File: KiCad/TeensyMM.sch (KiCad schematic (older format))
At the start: 13 parts, among them J1 MICROMOD-2222, U1 MK20DX256VLH7, U2 MKL02Z32VFG4, Y2 16MHz

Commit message: wip
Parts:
- removed JP1: SolderJumper_2_Open, Jumper:SolderJumper-2_P1.3mm_Open_RoundedPad1.0x1.5mm, symbol Jumper:SolderJumper_2_Open
- added JP1: SolderJumper_3_Open, Jumper:SolderJumper-3_P1.3mm_Open_RoundedPad1.0x1.5mm, symbol Jumper:SolderJumper_3_Open
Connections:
- net labels added: CTS, D3_CTX, D4_CRX, RTS
- net labels removed: EN
- wire segments 176 -> 181
- no-connect marks 44 -> 41
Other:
- note added: "Deactivates \nMKL02"
- note removed: "Close JP1 \nfor JTAG use\n(deactivates MKL02)"
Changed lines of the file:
@@
 Text GLabel 11600 4300 1    50   Input ~ 0
 SWD_DIO
-Text Notes 13100 4200 2    39   ~ 0
-Close JP1 \nfor JTAG use\n(deactivates MKL02)
+Text Notes 12700 4150 0    39   ~ 0
+Deactivates \nMKL02
 $Comp
 L power:GND #PWR013
@@
 	1    12800 4300
 	0    1    1    0
-$EndComp
-$Comp
-L Jumper:SolderJumper_2_Open JP1
-U 1 1 60214C71
-P 13000 4300
-F 0 "JP1" H 13000 4200 50  0000 C CNN
-F 1 "SolderJumper_2_Open" H 12450 4900 50  0001 C CNN
-F 2 "Jumper:SolderJumper-2_P1.3mm_Open_RoundedPad1.0x1.5mm" H 13000 4300 50  0001 C CNN
-F 3 "~" H 13000 4300 50  0001 C CNN
-	1    13000 4300
-	1    0    0    -1
 $EndComp
 Wire Wire Line
@@
 Text Label 10300 4900 0    50   ~ 0
 PTA7
-Wire Wire Line
-	13200 4300 13150 4300
-Wire Wire Line
-	12850 4300 12800 4300
-Text Label 13100 4300 0    50   ~ 0
-EN
 Text Label 10300 4700 0    50   ~ 0
 PTA6
@@
 NoConn ~ 4350 3400
 NoConn ~ 4350 3500
-NoConn ~ 4350 3900
-NoConn ~ 4350 4000
 NoConn ~ 4350 5500
 NoConn ~ 7950 3600
@@
 NoConn ~ 13200 4200
 NoConn ~ 13200 4400
-NoConn ~ 13200 4500
 NoConn ~ 13200 4700
 NoConn ~ 13200 5350
 NoConn ~ 13200 5450
+Text Label 2100 3200 0    50   ~ 0
+D3_CTX
+Text Label 2100 3300 0    50   ~ 0
+D4_CRX
+$Comp
+L Jumper:SolderJumper_3_Open JP1
+U 1 1 5FD8AAE7
+P 13000 4300
+F 0 "JP1" V 13100 4100 50  0000 L CNN
+F 1 "SolderJumper_3_Open" V 12350 3700 50  0001 L CNN
+F 2 "Jumper:SolderJumper-3_P1.3mm_Open_RoundedPad1.0x1.5mm" H 13000 4300 50  0001 C CNN
+F 3 "~" H 13000 4300 50  0001 C CNN
+	1    13000 4300
+	0    1    1    0
+$EndComp
+Wire Wire Line
+	13000 4500 13200 4500
+Wire Wire Line
+	12800 4300 12850 4300
+Wire Wire Line
+	13000 4100 13100 4100
+Wire Wire Line
+	13100 4100 13100 4300
+Wire Wire Line
+	13100 4300 13200 4300
+Wire Wire Line
+	4350 3900 4950 3900
+Wire Wire Line
+	4350 4000 4950 4000
+Text Label 4400 3900 0    50   ~ 0
+RTS
+Text Label 4400 4000 0    50   ~ 0
+CTS
 $EndSCHEMATC

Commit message: finalized 4layer design
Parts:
- removed Y2: 16MHz, Crystal:Crystal_SMD_3225-4Pin_3.2x2.5mm_HandSoldering, symbol Device:Crystal_GND24
- added JP2: SolderJumper_3_Bridged12, Jumper:SolderJumper-3_P1.3mm_Bridged12_RoundedPad1.0x1.5mm, symbol Jumper:SolderJumper_3_Bridged12
- added Y1: 16MHz, footprints:OSC_XRCHA16M000F0A01R0, symbol Device:Crystal_Small
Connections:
- net CTS is gone; now on net D32-CTS1: J1.15 (CTS1)
- net RTS is gone; now on net D25-RTS1: J1.13 (RTS1)
- net DAC: now reaches U1.18 (A14/DAC)
- net DAC: now also J1.32 (PWM0)
- net D26_A15-BAT_VIN3: now reaches U1.2 (D26/A15)
- net D26_A15-BAT_VIN3: now also J1.49 (BATT_VIN/3)
- net at U1.32 (OSC1): now also Y1.1
- net at U1.33 (OSC2): now also Y1.2
- net at D1.2 (A): now also JP2.2 (C); no longer U1.35 (D16/A2/TOUCH)
- net D17_A3: now reaches U1.36 (D17/A3/TOUCH)
- net D17_A3: now also J1.18 (D1/CAM_TRIG)
- net D32-CTS1: now reaches U1.41 (D32/PWM/TOUCH)
- net D25-RTS1: now reaches U1.42 (D25/PWM/TOUCH)
- net D22-A8: now reaches U1.44 (D22/A8/PWM/TOUCH)
- net D22-A8: now also J1.47 (PWM1)
- net D23: now reaches U1.45 (D23/A9/PWM/TOUCH)
- net D23: now also JP2.3 (B)
- net D28_A17: now reaches U1.53 (D28/A17)
- net D28_A17: now also J1.8 (G11)
- net D27_A16: now reaches U1.54 (D27/A16)
- net D27_A16: now also J1.67 (G8)
- net PTA1: now reaches JP1.1 (A), U2.15 (PTA1/IRQ_1/LPTMR0_ALT1)
- net PTA3: now reaches JP1.3 (B), U2.3 (PTA3)
- net D16_A2: now reaches J1.10 (D0)
- net D16_A2: now also U1.35 (D16/A2/TOUCH)
- net A10 renamed ADC0_N
- net ADC0_N: now also J1.63 (G10/ADC_D+/CAM_VSYNC); no longer J1.65 (G9/ADC_D-/CAM_HSYNC)
- net A11 renamed ADC0_P
- net ADC0_P: now also J1.65 (G9/ADC_D-/CAM_HSYNC); no longer J1.63 (G10/ADC_D+/CAM_VSYNC)
- net A12 renamed ADC1_N
- net ADC1_N: now also U1.12 (A13/ADC0_DM3); no longer U1.11 (A12/ADC0_DP3)
- net A13 renamed ADC1_P
- net ADC1_P: now also U1.11 (A12/ADC0_DP3); no longer U1.12 (A13/ADC0_DM3)
- net D0 renamed D00-RX1
- net D1 renamed D01-TX1
- net D10 renamed D10-TX2
- net D11 renamed D11-MOSI
- net D12 renamed D12-MISO
- net D13 renamed D13-SCK
- net D13-SCK: now also JP2.1 (A)
- net D14 renamed D14-PTD1
- net D15 renamed D15-CS
- net D18 renamed D18-SDA0
- net D19 renamed D19-SCL0
- net D2 renamed D02-PTD0
- net D20 renamed D20-PTD5
- net D21 renamed D21-PTD6
- net D24 renamed D24-I2C-INT
- net D29 renamed D29-SCL1
- net D30 renamed D30-SDA1
- net D3_CTX renamed D03-CAN-TX
- net D4_CRX renamed D04-CAN-TX
- net D5 renamed D05-PTD7
- net D6 renamed D06-PTD4
- net D7 renamed D07-PTD2
- net D8 renamed D08-PTD3
- net D9 renamed D09-RX2
- net RTC_3V: no longer names the net of J1.72 (RTC_3V)
- no-connect marks 41 -> 27
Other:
- note added: "Deactivate\nMKL02"
- note added: "Differential ADC\n(A12/A13)\n"
- note added: "Select LED pin\n(D13 or D23)"
- note added: "UART (2x)\n(Serial1 & Serial2)"
- note removed: "ADC (2x differential)"
- note removed: "Deactivates \nMKL02"
- note removed: "I2C (2x)"
- note removed: "UART (2x)"
- moved on the sheet: C1, C2, C3, C4, D1, J1, JP1, R1, R2, R3, U1, U2

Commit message: Added RTC crystal, and v_bat circuitry. Needs cleanup
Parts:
- added D2: D_Schottky_x2_KCom_AAK, Package_TO_SOT_SMD:SOT-23, symbol Device:D_Schottky_x2_KCom_AAK
- added Y2: 16MHz, footprints:OSC_XRCHA16M000F0A01R0, symbol Device:Crystal_Small
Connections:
- net +3V3: now also D2.1 (A); no longer U1.21 (VBAT)
- net at U1.19 (XTAL32): now also Y2.1
- net at U1.20 (EXTAL32): now also Y2.2
- net RTC3V: now reaches J1.72 (RTC_3V)
- net RTC3V: now also D2.2 (A)
- new net: D2.3 (K), U1.21 (VBAT)
- no-connect marks 27 -> 24
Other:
- note removed: "RTC not yet\nimplemented"
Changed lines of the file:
@@
 PTD0 - PTD7
 Wire Wire Line
-	9375 3450 9475 3450
+	9375 3450 9425 3450
 Wire Wire Line
 	9375 1750 9425 1750
@@
 Text Notes 12775 5850 0    50   ~ 0
 PJRC Bootloader
-Wire Wire Line
-	9375 3050 9375 3150
-Connection ~ 9375 3150
 $Comp
 L power:+3.3V #PWR09
@@
 $EndComp
 $Comp
-L power:GND #PWR010
-U 1 1 5FE1A18E
-P 9375 3200
-F 0 "#PWR010" H 9375 2950 50  0001 C CNN
-F 1 "GND" H 9575 3200 50  0000 R CNN
-F 2 "" H 9375 3200 50  0001 C CNN
-F 3 "" H 9375 3200 50  0001 C CNN
-	1    9375 3200
-	1    0    0    -1
-$EndComp
-$Comp
 L power:GND #PWR07
 U 1 1 5FEC0EED
 P 9475 3450
 F 0 "#PWR07" H 9475 3200 50  0001 C CNN
-F 1 "GND" V 9480 3322 50  0000 R CNN
+F 1 "GND" V 9575 3350 50  0000 R CNN
 F 2 "" H 9475 3450 50  0001 C CNN
 F 3 "" H 9475 3450 50  0001 C CNN
@@
 	0    -1   -1   0
 $EndComp
-$Comp
-L power:+3.3V #PWR015
-U 1 1 5FFF94FE
-P 9475 3650
-F 0 "#PWR015" H 9475 3500 50  0001 C CNN
-F 1 "+3.3V" V 9475 3775 50  0000 L CNN
-F 2 "" H 9475 3650 50  0001 C CNN
-F 3 "" H 9475 3650 50  0001 C CNN
-	1    9475 3650
-	0    1    1    0
-$EndComp
 Wire Wire Line
 	9375 2150 9425 2150
@@
 Wire Wire Line
 	9375 2250 9425 2250
-Wire Wire Line
-	9375 3150 9375 3200
 Wire Wire Line
 	9425 2050 9425 2150
@@
 Text Notes 9775 2950 1    39   ~ 0
 Very simplistic analog \nreferencing, but should \nwork somehow. Might \nimprove later if the board \nworks at all.
-Text Notes 9475 4000 0    39   ~ 0
-RTC not yet\nimplemented
 Wire Wire Line
 	12325 3700 12275 3700
@@
 Wire Wire Line
 	2525 4950 2675 4950
-Wire Wire Line
-	9375 3650 9475 3650
 NoConn ~ 2675 2150
-NoConn ~ 2675 2250
 Text GLabel 7075 3950 0    50   Input ~ 0
 D23
-NoConn ~ 9375 3850
-NoConn ~ 9375 4050
 $Comp
 L power:PWR_FLAG #FLG0101
@@
 Wire Wire Line
 	12125 2350 12225 2350
+$Comp
+L Device:Crystal_Small Y2
+U 1 1 604324EE
+P 9500 3950
+F 0 "Y2" V 9454 4038 50  0000 L CNN
+F 1 "16MHz" V 9545 4038 50  0000 L CNN
+F 2 "footprints:OSC_XRCHA16M000F0A01R0" H 9500 3950 50  0001 C CNN
+F 3 "~" H 9500 3950 50  0001 C CNN
+	1    9500 3950
+	0    1    1    0
+$EndComp
+Wire Wire Line
+	9375 3850 9500 3850
+Wire Wire Line
+	9375 4050 9500 4050
+$Comp
+L Device:D_Schottky_x2_KCom_AAK D2
+U 1 1 6046754E
+P 9975 3650
+F 0 "D2" V 9929 3729 50  0000 L CNN
+F 1 "D_Schottky_x2_KCom_AAK" V 9525 3650 50  0000 L CNN
+F 2 "Package_TO_SOT_SMD:SOT-23" H 9975 3650 50  0001 C CNN
+F 3 "~" H 9975 3650 50  0001 C CNN
+	1    9975 3650
+	0    1    1    0
+$EndComp
+$Comp
+L power:+3.3V #PWR0102
+U 1 1 6046F42E
+P 10075 3350
+F 0 "#PWR0102" H 10075 3200 50  0001 C CNN
+F 1 "+3.3V" V 10000 3225 50  0000 L CNN
+F 2 "" H 10075 3350 50  0001 C CNN
+F 3 "" H 10075 3350 50  0001 C CNN
+	1    10075 3350
+	0    1    1    0
+$EndComp
+Text GLabel 2575 2250 0    50   Input ~ 0
+RTC3V
+Wire Wire Line
+	2575 2250 2675 2250
+Text GLabel 10075 3950 2    50   Input ~ 0
+RTC3V
+Wire Wire Line
+	9975 3950 10075 3950
+Wire Wire Line
+	9375 3650 9775 3650
+Wire Wire Line
+	9975 3350 10075 3350
+Wire Wire Line
+	9375 3050 9425 3050
+Wire Wire Line
+	9425 3050 9425 3150
+Connection ~ 9425 3450
+Wire Wire Line
+	9425 3450 9475 3450
+Wire Wire Line
+	9375 3150 9425 3150
+Connection ~ 9425 3150
+Wire Wire Line
+	9425 3150 9425 3450
 $EndSCHEMATC

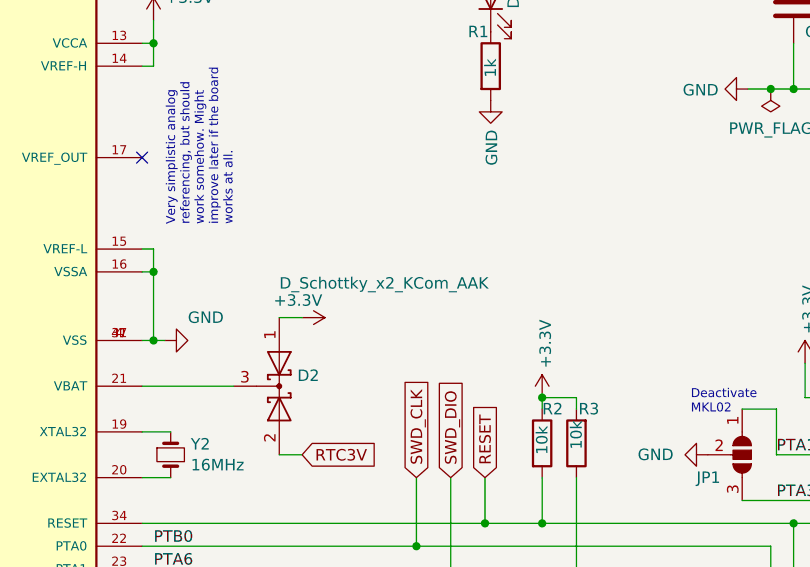
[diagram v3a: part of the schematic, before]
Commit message: Cleanup board and gerbers
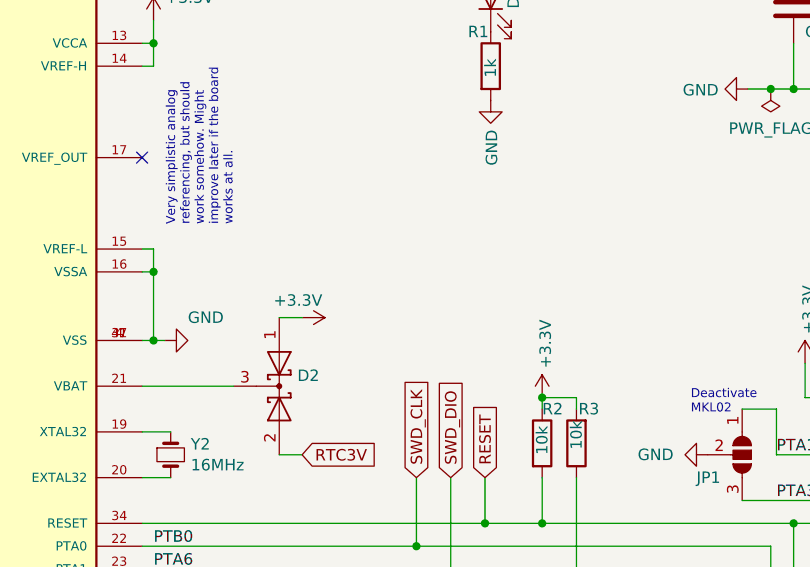
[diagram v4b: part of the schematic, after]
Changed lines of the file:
@@
 P 9975 3650
 F 0 "D2" V 9929 3729 50  0000 L CNN
-F 1 "D_Schottky_x2_KCom_AAK" V 9525 3650 50  0000 L CNN
+F 1 "D_Schottky_x2_KCom_AAK" V 9525 3650 50  0001 L CNN
 F 2 "Package_TO_SOT_SMD:SOT-23" H 9975 3650 50  0001 C CNN
 F 3 "~" H 9975 3650 50  0001 C CNN
